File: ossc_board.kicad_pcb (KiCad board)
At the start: 2 copper layers, 124.6 x 68.7 mm, 230 parts, among them J1 VGA, J2 3XRCA_CONN, J3 JP21, J4 HDMI_CONN, J5 5VDC_IN, J6 SJ1-3533NG, J7 SJ1-3533NG, P1 JTAG_CONN, P3 mSD_CONN, Q1 BC847, Q2 BC857, SW1 SPST, SW2 SW_PUSH, SW3 SW_PUSH, SW4 DPDT, U1 TVP7002PZP, U10 S25FL216K, U11 IRM-V538/TR1, U12 TLV70012, U13 TLV70025, U14 TLV70012, U15 TLV70018, U16 TLV70018, U17 THS7353, U2 EP4CE15E22, U3 IT6613, U4 SN74LVC2G17, U5 AP7361C, U6 TLV70033, U7 NCP703SN19T1G, U8 PCM1862, U9 TLV70019, Y1 ACHL-27MHZ-EK, Y2 24.576MHz

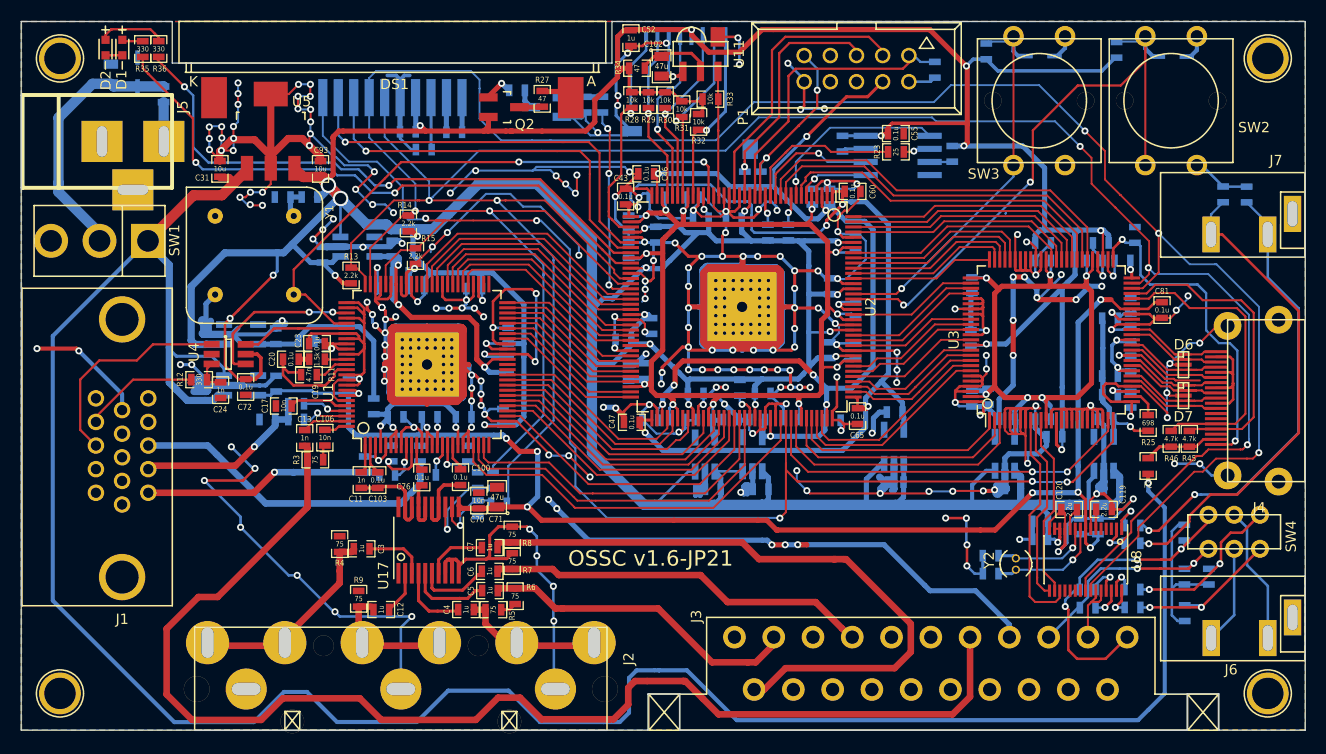
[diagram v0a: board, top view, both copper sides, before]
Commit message: Regenerate PCB files after recent small updates.
- update R12 value on schematic, netlist and layout.
- update ECS-3X9X footprint.
- add pdf of the schematic.
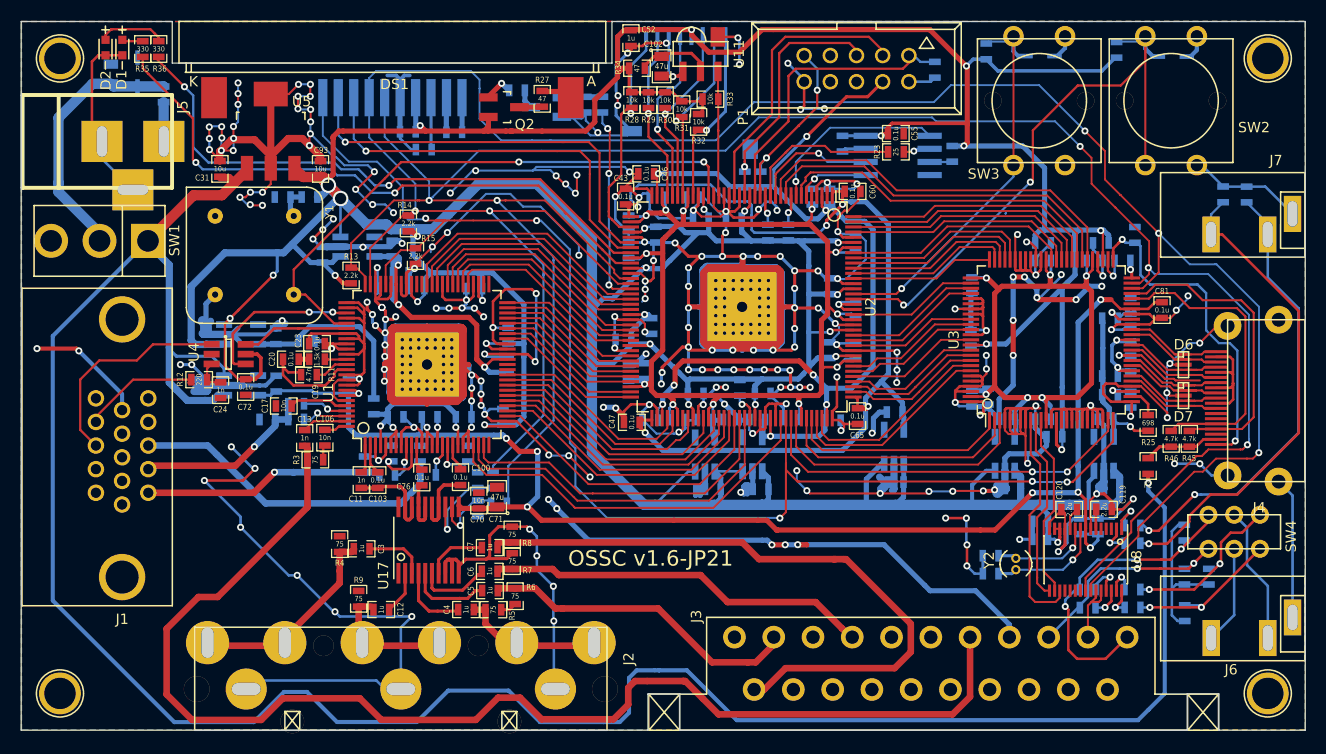
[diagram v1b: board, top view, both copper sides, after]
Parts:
- R12: value 330 -> 220
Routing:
- net GND: track 1319.2 -> 1369.8 mm
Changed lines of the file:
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@@
     (links 838)
     (no_connects 0)
-    (area 7.070879 14.225 132.221001 86.31072)
+    (area 7.313799 16.967099 131.984001 85.814001)
     (thickness 1.6)
-    (drawings 17)
-    (tracks 4138)
+    (drawings 35)
+    (tracks 4152)
     (zones 0)
     (modules 230)
@@
       (effects (font (size 0.5842 0.508) (thickness 0.127)))
     )
-    (fp_text value 330 (at 0 0 270) (layer F.SilkS)
+    (fp_text value 220 (at 0 0 270) (layer F.SilkS)
       (effects (font (size 0.508 0.4572) (thickness 0.1143)))
     )
@@
     (at 101.42 70.58 180)
     (attr smd)
-    (fp_text reference C111 (at -1.85 -0.22 450) (layer B.SilkS)
+    (fp_text reference C111 (at 1.75 -0.43 450) (layer B.SilkS)
       (effects (font (size 0.5842 0.508) (thickness 0.127)) (justify mirror))
     )
@@
     (at 101.41 68.84 180)
     (attr smd)
-    (fp_text reference C112 (at -1.81 0.31 450) (layer B.SilkS)
+    (fp_text reference C112 (at 1.76 0.1 450) (layer B.SilkS)
       (effects (font (size 0.5842 0.508) (thickness 0.127)) (justify mirror))
     )
@@
     )
   )
-  (module custom_components:ECS-3X9X (layer F.Cu)
-    (at 103.861 69.647 90)
-    (descr "Crystal, Quarz, Rundgehaeuse, round, vertical, stehend, Uhrenquarz, Diam. 3mm,")
-    (tags "Crystal Quarz Rundgehaeuse round vertical stehend Uhrenquarz Diam. 3mm")
-    (fp_text reference Y2 (at 0.36576 -2.59842 90) (layer F.SilkS)
-      (effects (font (size 1 1) (thickness 0.15)))
-    )
-    (fp_text value 24.576MHz (at 0.2413 2.5146 90) (layer F.Fab)
-      (effects (font (size 1 1) (thickness 0.15)))
-    )
-    (fp_line (start 1.30048 0.89916) (end 1.04902 1.15062) (layer F.SilkS) (width 0.15))
-    (fp_line (start 1.04902 1.15062) (end 0.70104 1.39954) (layer F.SilkS) (width 0.15))
-    (fp_line (start 0.70104 1.39954) (end 0.14986 1.5494) (layer F.SilkS) (width 0.15))
-    (fp_line (start 0.14986 1.5494) (end -0.24892 1.5494) (layer F.SilkS) (width 0.15))
-    (fp_line (start -0.24892 1.5494) (end -0.7493 1.34874) (layer F.SilkS) (width 0.15))
-    (fp_line (start -0.7493 1.34874) (end -1.15062 1.00076) (layer F.SilkS) (width 0.15))
-    (fp_line (start 1.30048 -0.8509) (end 1.15062 -1.04902) (layer F.SilkS) (width 0.15))
-    (fp_line (start 1.15062 -1.04902) (end 0.8509 -1.30048) (layer F.SilkS) (width 0.15))
-    (fp_line (start 0.8509 -1.30048) (end 0.39878 -1.50114) (layer F.SilkS) (width 0.15))
-    (fp_line (start 0.39878 -1.50114) (end -0.0508 -1.5494) (layer F.SilkS) (width 0.15))
-    (fp_line (start -0.0508 -1.5494) (end -0.55118 -1.45034) (layer F.SilkS) (width 0.15))
-    (fp_line (start -0.55118 -1.45034) (end -0.89916 -1.24968) (layer F.SilkS) (width 0.15))
-    (fp_line (start -0.89916 -1.24968) (end -1.24968 -0.89916) (layer F.SilkS) (width 0.15))
-    (pad 1 thru_hole circle (at -0.55 0 90) (size 0.8 0.8) (drill 0.5) (layers *.Cu *.Mask F.SilkS)
-      (net 204 "Net-(C111-Pad1)"))
-    (pad 2 thru_hole circle (at 0.55 0 90) (size 0.8 0.8) (drill 0.5) (layers *.Cu *.Mask F.SilkS)
-      (net 205 "Net-(C112-Pad1)"))
-  )
   (module custom_components:SLP2510P8 (layer F.Cu)
     (at 120.12 53.31 270)
@@
       (net 107 GND))
   )
+  (module custom_components:ECS-3X9X (layer F.Cu)
+    (at 103.861 69.647 90)
+    (descr "Crystal, Quarz, Rundgehaeuse, round, vertical, stehend, Uhrenquarz, Diam. 3mm,")
+    (tags "Crystal Quarz Rundgehaeuse round vertical stehend Uhrenquarz Diam. 3mm")
+    (fp_text reference Y2 (at 0.36576 -2.59842 90) (layer F.SilkS)
+      (effects (font (size 1 1) (thickness 0.15)))
+    )
+    (fp_text value 24.576MHz (at 0.2413 2.5146 90) (layer F.Fab)
+      (effects (font (size 1 1) (thickness 0.15)))
+    )
+    (fp_line (start 1.30048 0.89916) (end 1.04902 1.15062) (layer F.SilkS) (width 0.15))
+    (fp_line (start 1.04902 1.15062) (end 0.70104 1.39954) (layer F.SilkS) (width 0.15))
+    (fp_line (start 0.70104 1.39954) (end 0.14986 1.5494) (layer F.SilkS) (width 0.15))
+    (fp_line (start 0.14986 1.5494) (end -0.24892 1.5494) (layer F.SilkS) (width 0.15))
+    (fp_line (start -0.24892 1.5494) (end -0.7493 1.34874) (layer F.SilkS) (width 0.15))
+    (fp_line (start -0.7493 1.34874) (end -1.15062 1.00076) (layer F.SilkS) (width 0.15))
+    (fp_line (start 1.30048 -0.8509) (end 1.15062 -1.04902) (layer F.SilkS) (width 0.15))
+    (fp_line (start 1.15062 -1.04902) (end 0.8509 -1.30048) (layer F.SilkS) (width 0.15))
+    (fp_line (start 0.8509 -1.30048) (end 0.39878 -1.50114) (layer F.SilkS) (width 0.15))
+    (fp_line (start 0.39878 -1.50114) (end -0.0508 -1.5494) (layer F.SilkS) (width 0.15))
+    (fp_line (start -0.0508 -1.5494) (end -0.55118 -1.45034) (layer F.SilkS) (width 0.15))
+    (fp_line (start -0.55118 -1.45034) (end -0.89916 -1.24968) (layer F.SilkS) (width 0.15))
+    (fp_line (start -0.89916 -1.24968) (end -1.24968 -0.89916) (layer F.SilkS) (width 0.15))
+    (pad 1 thru_hole circle (at -0.55 0 90) (size 0.9 0.9) (drill 0.5) (layers *.Cu *.Mask F.SilkS)
+      (net 204 "Net-(C111-Pad1)"))
+    (pad 2 thru_hole circle (at 0.55 0 90) (size 0.9 0.9) (drill 0.5) (layers *.Cu *.Mask F.SilkS)
+      (net 205 "Net-(C112-Pad1)"))
+  )
   (gr_line (start 58.386 81.7762) (end 60.006 81.7762) (layer Edge.Cuts) (width 1.2))
   (gr_line (start 62.946 76.376) (end 62.946 78.176) (layer Edge.Cuts) (width 1.2))
@@
   (segment (start 51.7398 59.5398) (end 51.7398 58.039) (width 0.18) (layer F.Cu) (net 106))
   (segment (start 61.3156 63.5) (end 60.9588 63.1432) (width 0.18) (layer F.Cu) (net 106))
+  (segment (start 130.706 74.83) (end 130.706 63.006) (width 0.25) (layer B.Cu) (net 107))
+  (segment (start 130.706 63.006) (end 129.35 61.65) (width 0.25) (layer B.Cu) (net 107))
+  (segment (start 15.549 20.2943) (end 14.8457 20.2943) (width 0.25) (layer F.Cu) (net 107))
+  (segment (start 14.23 20.91) (end 14.23 27.67634) (width 0.25) (layer F.Cu) (net 107))
+  (segment (start 14.8457 20.2943) (end 14.23 20.91) (width 0.25) (layer F.Cu) (net 107))
+  (segment (start 14.23 27.67634) (end 15.20266 28.649) (width 0.25) (layer F.Cu) (net 107))
+  (segment (start 15.20266 28.649) (end 15.20266 30.34826) (width 0.25) (layer B.Cu) (net 107))
+  (segment (start 15.20266 30.34826) (end 18.2024 33.348) (width 0.25) (layer B.Cu) (net 107))
+  (segment (start 44.196 81.7762) (end 42.6562 81.7762) (width 0.25) (layer B.Cu) (net 107))
+  (segment (start 42.6562 81.7762) (end 41.82 80.94) (width 0.25) (layer B.Cu) (net 107))
+  (segment (start 41.82 80.94) (end 30.0322 80.94) (width 0.25) (layer B.Cu) (net 107))
+  (segment (start 30.0322 80.94) (end 29.196 81.7762) (width 0.25) (layer B.Cu) (net 107))
+  (segment (start 126.25 33.038) (end 128.06 33.038) (width 0.25) (layer B.Cu) (net 107))
+  (segment (start 128.06 33.038) (end 130.698 35.676) (width 0.25) (layer B.Cu) (net 107))
   (segment (start 95.02 71.718) (end 91.074 67.772) (width 0.5) (layer B.Cu) (net 107))
   (segment (start 95.542 72.24) (end 95.02 71.718) (width 0.5) (layer B.Cu) (net 107))
